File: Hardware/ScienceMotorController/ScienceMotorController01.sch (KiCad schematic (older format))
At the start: 14 parts

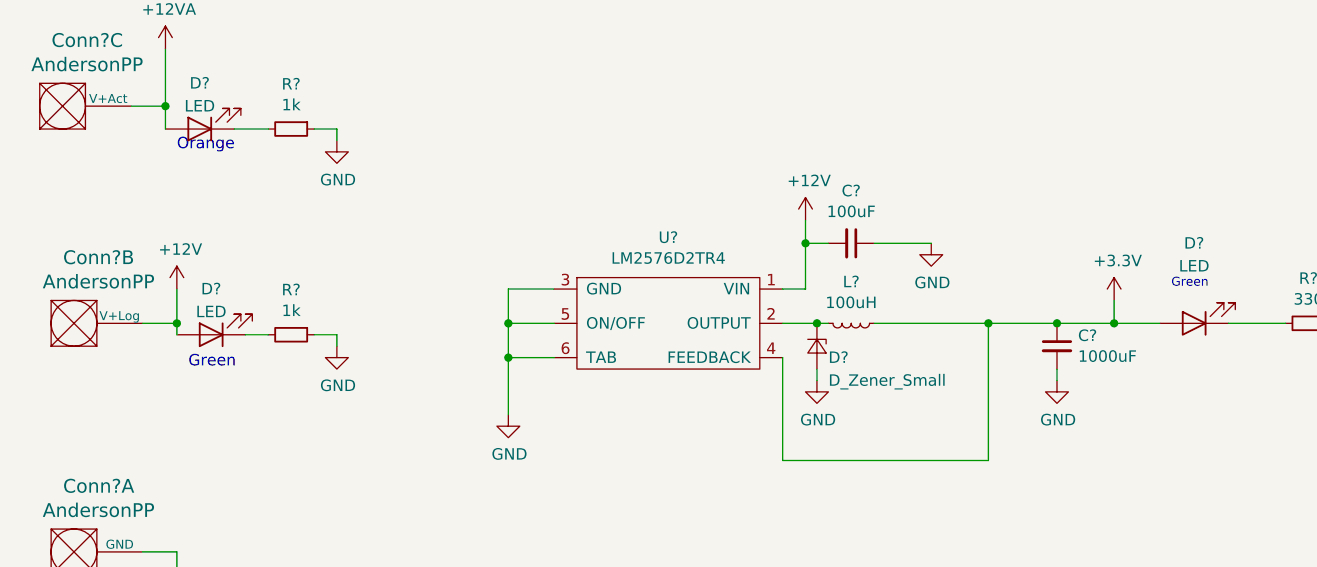
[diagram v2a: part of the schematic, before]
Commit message: changed everything to actuation, added schottky diode, added A/B flags to tiva
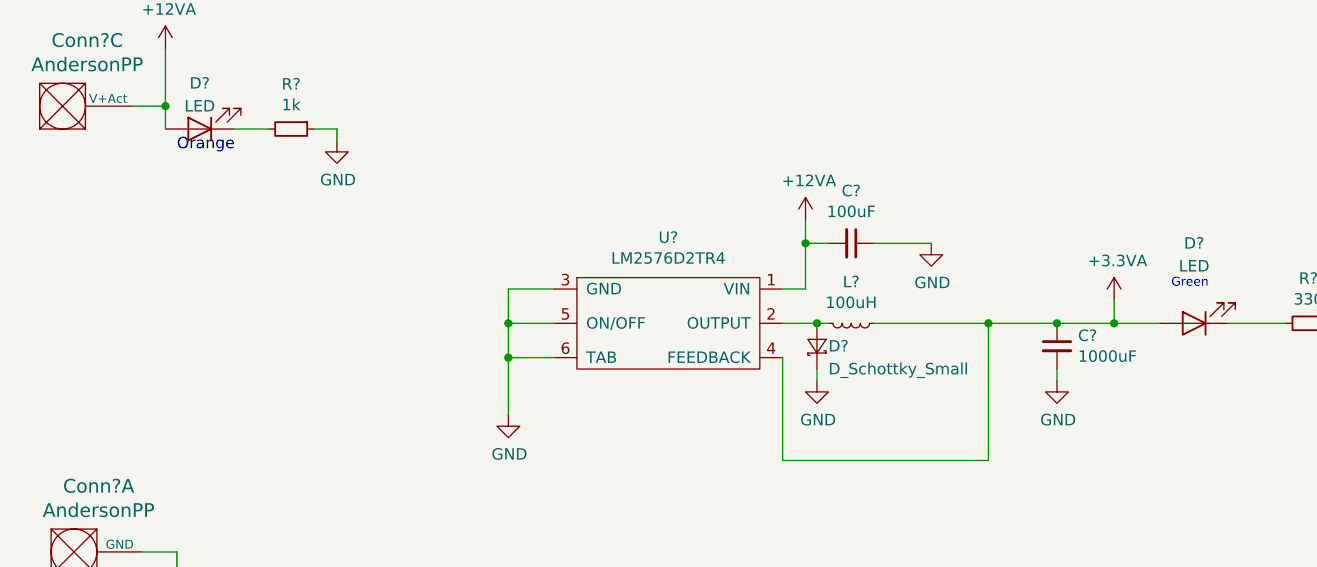
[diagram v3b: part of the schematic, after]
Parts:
- removed Conn?: AndersonPP, symbol MRDT_Connectors:AndersonPP
- removed D?: D_Zener_Small, symbol Device:D_Zener_Small
- removed D?: LED, symbol Device:LED
- removed R?: 1k, symbol Device:R_Small
- added D?: D_Schottky_Small, symbol Device:D_Schottky_Small
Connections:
- net +12V is gone; now on net +12VA: C?.2, U?.1 (VIN)
- net GND: now also D?.1 (K)
- net at L?.2, U?.2 (OUTPUT): now also D?.2 (A)
- net +3V3 renamed +3.3VA
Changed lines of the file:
@@
-$Comp
-L MRDT_Connectors:AndersonPP Conn?
-U 2 1 5F6E2CCA
-P 750 2000
-F 0 "Conn?" H 958 2387 60  0000 C CNN
-F 1 "AndersonPP" H 958 2281 60  0000 C CNN
-F 2 "" H 600 1450 60  0001 C CNN
-F 3 "" H 600 1450 60  0001 C CNN
-	2    750  2000
-	1    0    0    -1
-$EndComp
 $Comp
 L MRDT_Connectors:AndersonPP Conn?
@@
 	1    0    0    -1
 $EndComp
-$Comp
-L power:+12V #PWR?
-U 1 1 5F6E992B
-P 1300 1750
-F 0 "#PWR?" H 1300 1600 50  0001 C CNN
-F 1 "+12V" H 1315 1923 50  0000 C CNN
-F 2 "" H 1300 1750 50  0001 C CNN
-F 3 "" H 1300 1750 50  0001 C CNN
-	1    1300 1750
-	1    0    0    -1
-$EndComp
-Wire Wire Line
-	1150 1900 1300 1900
 Wire Wire Line
 	1300 3100 1300 2900
@@
 F 3 "" H 2750 2300 50  0001 C CNN
 	1    2750 2300
-	1    0    0    -1
-$EndComp
-$Comp
-L power:+12V #PWR?
-U 1 1 5F6EEFCA
-P 4050 1450
-F 0 "#PWR?" H 4050 1300 50  0001 C CNN
-F 1 "+12V" H 4065 1623 50  0000 C CNN
-F 2 "" H 4050 1450 50  0001 C CNN
-F 3 "" H 4050 1450 50  0001 C CNN
-	1    4050 1450
 	1    0    0    -1
 $EndComp
@@
 	4350 1550 4600 1550
 $Comp
-L Device:D_Zener_Small D?
-U 1 1 5F6F8DDF
-P 4100 2000
-F 0 "D?" V 4150 2050 50  0000 L CNN
-F 1 "D_Zener_Small" V 4250 2050 50  0000 L CNN
-F 2 "" V 4100 2000 50  0001 C CNN
-F 3 "~" V 4100 2000 50  0001 C CNN
-	1    4100 2000
-	0    1    1    0
-$EndComp
-$Comp
 L Device:L_Small L?
 U 1 1 5F6FA71E
@@
 $EndComp
 Wire Wire Line
-	3950 1900 4100 1900
-Wire Wire Line
 	4050 1450 4050 1550
 Wire Wire Line
@@
 Wire Wire Line
 	5150 2100 5150 2150
-Connection ~ 4100 1900
-Wire Wire Line
-	4100 1900 4150 1900
 Wire Wire Line
 	3950 2050 3950 2500
@@
 	5400 1900 5150 1900
 Connection ~ 5150 1900
-$Comp
-L power:+3.3V #PWR?
-U 1 1 5F70AA1A
-P 5400 1800
-F 0 "#PWR?" H 5400 1650 50  0001 C CNN
-F 1 "+3.3V" H 5415 1973 50  0000 C CNN
-F 2 "" H 5400 1800 50  0001 C CNN
-F 3 "" H 5400 1800 50  0001 C CNN
-	1    5400 1800
-	1    0    0    -1
-$EndComp
 Wire Wire Line
 	5400 1800 5400 1900
@@
 Text Notes 1300 1150 0    50   ~ 0
 Orange
-$Comp
-L Device:LED D?
-U 1 1 5F7C0921
-P 1450 1950
-F 0 "D?" H 1450 1750 50  0000 C CNN
-F 1 "LED" H 1450 1850 50  0000 C CNN
-F 2 "" H 1450 1950 50  0001 C CNN
-F 3 "~" H 1450 1950 50  0001 C CNN
-	1    1450 1950
-	-1   0    0    1
-$EndComp
-Wire Wire Line
-	1300 1750 1300 1900
-Connection ~ 1300 1900
-Wire Wire Line
-	1300 1900 1300 1950
-$Comp
-L Device:R_Small R?
-U 1 1 5F7CD72E
-P 1800 1950
-F 0 "R?" V 1604 1950 50  0000 C CNN
-F 1 "1k" V 1695 1950 50  0000 C CNN
-F 2 "" H 1800 1950 50  0001 C CNN
-F 3 "~" H 1800 1950 50  0001 C CNN
-	1    1800 1950
-	0    1    1    0
-$EndComp
-Wire Wire Line
-	1700 1950 1600 1950
-$Comp
-L power:GND #PWR?
-U 1 1 5F7CEAC2
-P 2000 2000
-F 0 "#PWR?" H 2000 1750 50  0001 C CNN
-F 1 "GND" H 2005 1827 50  0000 C CNN
-F 2 "" H 2000 2000 50  0001 C CNN
-F 3 "" H 2000 2000 50  0001 C CNN
-	1    2000 2000
-	1    0    0    -1
-$EndComp
-Wire Wire Line
-	1900 1950 2000 1950
-Wire Wire Line
-	2000 1950 2000 2000
-Text Notes 1350 2100 0    50   ~ 0
-Green
+Wire Wire Line
+	3950 1900 4100 1900
+$Comp
+L Device:D_Schottky_Small D?
+U 1 1 5F80E7DD
+P 4100 2000
+F 0 "D?" V 4100 1950 50  0000 R CNN
+F 1 "D_Schottky_Small" V 4000 1950 50  0000 R CNN
+F 2 "" V 4100 2000 50  0001 C CNN
+F 3 "~" V 4100 2000 50  0001 C CNN
+	1    4100 2000
+	0    -1   -1   0
+$EndComp
+Connection ~ 4100 1900
+Wire Wire Line
+	4100 1900 4150 1900
+$Comp
+L power:+12VA #PWR?
+U 1 1 5F80FF5E
+P 4050 1450
+F 0 "#PWR?" H 4050 1300 50  0001 C CNN
+F 1 "+12VA" H 4065 1623 50  0000 C CNN
+F 2 "" H 4050 1450 50  0001 C CNN
+F 3 "" H 4050 1450 50  0001 C CNN
+	1    4050 1450
+	1    0    0    -1
+$EndComp
+$Comp
+L power:+3.3VA #PWR?
+U 1 1 5F81167B
+P 5400 1800
+F 0 "#PWR?" H 5400 1650 50  0001 C CNN
+F 1 "+3.3VA" H 5415 1973 50  0000 C CNN
+F 2 "" H 5400 1800 50  0001 C CNN
+F 3 "" H 5400 1800 50  0001 C CNN
+	1    5400 1800
+	1    0    0    -1
+$EndComp
 $EndSCHEMATC

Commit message: schematic review
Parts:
- removed Conn? (x2): AndersonPP, symbol MRDT_Connectors:AndersonPP
- removed D?: LED, symbol Device:LED
- removed R?: 1k, symbol Device:R_Small
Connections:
- net GND: now also D?.2 (A); no longer D?.1 (K)
- net at L?.2, U?.2 (OUTPUT): now also D?.1 (K); no longer D?.2 (A)
- net +12VA renamed 12VA
- net +3.3VA renamed 3.3VA
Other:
- note removed: "Orange"
- note removed: "Reminder:\nNeed High Current 10A bus\nNeed Low Current 3A bus"
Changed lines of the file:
@@
 $Descr A4 11693 8268
 encoding utf-8
-Sheet 2 11
+Sheet 2 10
 Title ""
 Date ""
@@
 Comment4 ""
 $EndDescr
-$Comp
-L MRDT_Connectors:AndersonPP Conn?
-U 1 1 5F6E39B8
-P 750 3000
-F 0 "Conn?" H 958 3387 60  0000 C CNN
-F 1 "AndersonPP" H 958 3281 60  0000 C CNN
-F 2 "" H 600 2450 60  0001 C CNN
-F 3 "" H 600 2450 60  0001 C CNN
-	1    750  3000
-	1    0    0    -1
-$EndComp
 Text Notes 7100 7000 0    315  ~ 0
 Sheet 01: Power
@@
 	1    0    0    -1
 $EndComp
-$Comp
-L power:GND #PWR?
-U 1 1 5F6E83C1
-P 1300 3100
-F 0 "#PWR?" H 1300 2850 50  0001 C CNN
-F 1 "GND" H 1305 2927 50  0000 C CNN
-F 2 "" H 1300 3100 50  0001 C CNN
-F 3 "" H 1300 3100 50  0001 C CNN
-	1    1300 3100
-	1    0    0    -1
-$EndComp
-Wire Wire Line
-	1300 3100 1300 2900
-Wire Wire Line
-	1300 2900 1150 2900
 Wire Wire Line
 	2950 1750 2750 1750
@@
 Wire Wire Line
 	6450 1900 6450 2150
-Text Notes 7100 1600 0    79   ~ 0
-Reminder:\nNeed High Current 10A bus\nNeed Low Current 3A bus
-$Comp
-L MRDT_Connectors:AndersonPP Conn?
-U 3 1 5F759AF7
-P 700 1050
-F 0 "Conn?" H 908 1437 60  0000 C CNN
-F 1 "AndersonPP" H 908 1331 60  0000 C CNN
-F 2 "" H 550 500 60  0001 C CNN
-F 3 "" H 550 500 60  0001 C CNN
-	3    700  1050
-	1    0    0    -1
-$EndComp
-Wire Wire Line
-	1100 950  1250 950
-Wire Wire Line
-	1250 950  1250 700
-$Comp
-L power:+12VA #PWR?
-U 1 1 5F75C024
-P 1250 700
-F 0 "#PWR?" H 1250 550 50  0001 C CNN
-F 1 "+12VA" H 1265 873 50  0000 C CNN
-F 2 "" H 1250 700 50  0001 C CNN
-F 3 "" H 1250 700 50  0001 C CNN
-	1    1250 700
-	1    0    0    -1
-$EndComp
-$Comp
-L Device:LED D?
-U 1 1 5F7BA809
-P 1400 1050
-F 0 "D?" H 1400 850 50  0000 C CNN
-F 1 "LED" H 1400 950 50  0000 C CNN
-F 2 "" H 1400 1050 50  0001 C CNN
-F 3 "~" H 1400 1050 50  0001 C CNN
-	1    1400 1050
-	-1   0    0    1
-$EndComp
-Wire Wire Line
-	1250 1050 1250 950
-Connection ~ 1250 950
-$Comp
-L Device:R_Small R?
-U 1 1 5F7BD886
-P 1800 1050
-F 0 "R?" V 1604 1050 50  0000 C CNN
-F 1 "1k" V 1695 1050 50  0000 C CNN
-F 2 "" H 1800 1050 50  0001 C CNN
-F 3 "~" H 1800 1050 50  0001 C CNN
-	1    1800 1050
-	0    1    1    0
-$EndComp
-Wire Wire Line
-	1550 1050 1700 1050
-$Comp
-L power:GND #PWR?
-U 1 1 5F7BF549
-P 2000 1100
-F 0 "#PWR?" H 2000 850 50  0001 C CNN
-F 1 "GND" H 2005 927 50  0000 C CNN
-F 2 "" H 2000 1100 50  0001 C CNN
-F 3 "" H 2000 1100 50  0001 C CNN
-	1    2000 1100
-	1    0    0    -1
-$EndComp
-Wire Wire Line
-	1900 1050 2000 1050
-Wire Wire Line
-	2000 1050 2000 1100
-Text Notes 1300 1150 0    50   ~ 0
-Orange
-Wire Wire Line
-	3950 1900 4100 1900
 $Comp
 L Device:D_Schottky_Small D?
 U 1 1 5F80E7DD
 P 4100 2000
-F 0 "D?" V 4100 1950 50  0000 R CNN
-F 1 "D_Schottky_Small" V 4000 1950 50  0000 R CNN
+F 0 "D?" V 4200 2200 50  0000 R CNN
+F 1 "D_Schottky_Small" V 4100 2650 50  0000 R CNN
 F 2 "" V 4100 2000 50  0001 C CNN
 F 3 "~" V 4100 2000 50  0001 C CNN
 	1    4100 2000
-	0    -1   -1   0
-$EndComp
+	0    1    1    0
+$EndComp
+Wire Wire Line
+	3950 1900 4100 1900
 Connection ~ 4100 1900
 Wire Wire Line
 	4100 1900 4150 1900
-$Comp
-L power:+12VA #PWR?
-U 1 1 5F80FF5E
-P 4050 1450
-F 0 "#PWR?" H 4050 1300 50  0001 C CNN
-F 1 "+12VA" H 4065 1623 50  0000 C CNN
-F 2 "" H 4050 1450 50  0001 C CNN
-F 3 "" H 4050 1450 50  0001 C CNN
-	1    4050 1450
-	1    0    0    -1
-$EndComp
-$Comp
-L power:+3.3VA #PWR?
-U 1 1 5F81167B
-P 5400 1800
-F 0 "#PWR?" H 5400 1650 50  0001 C CNN
-F 1 "+3.3VA" H 5415 1973 50  0000 C CNN
-F 2 "" H 5400 1800 50  0001 C CNN
-F 3 "" H 5400 1800 50  0001 C CNN
-	1    5400 1800
-	1    0    0    -1
-$EndComp
+Text HLabel 4050 1450 1    50   Input ~ 0
+12VA
+Text HLabel 5400 1800 1    50   Output ~ 0
+3.3VA
 $EndSCHEMATC
